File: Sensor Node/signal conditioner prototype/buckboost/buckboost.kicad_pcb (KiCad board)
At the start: 2 copper layers, 25.4 x 16 mm, 12 parts, among them J1 Conn_01x03_Pin, U9 TPS63000

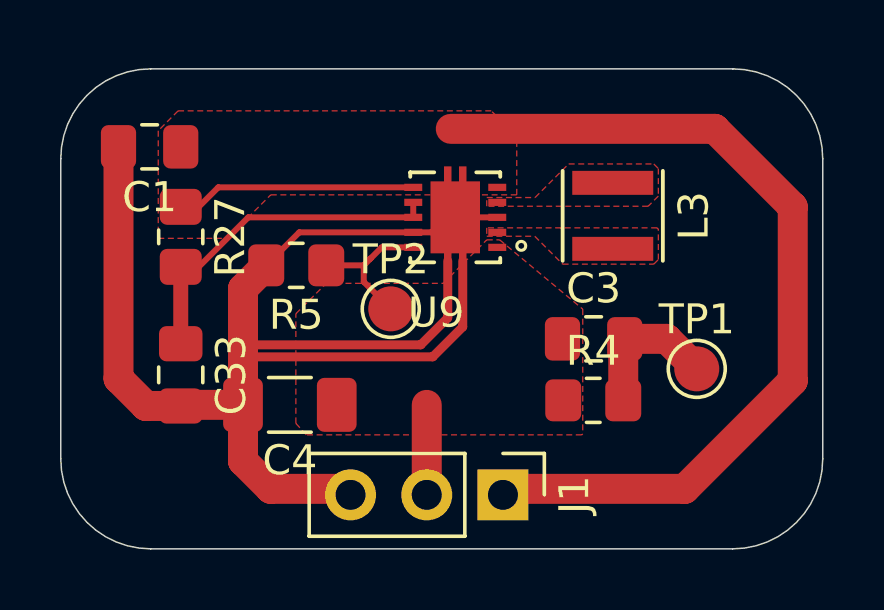
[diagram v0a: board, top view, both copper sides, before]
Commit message: Add finalized firmware - implemented power savings mode and implemented complete FSM.
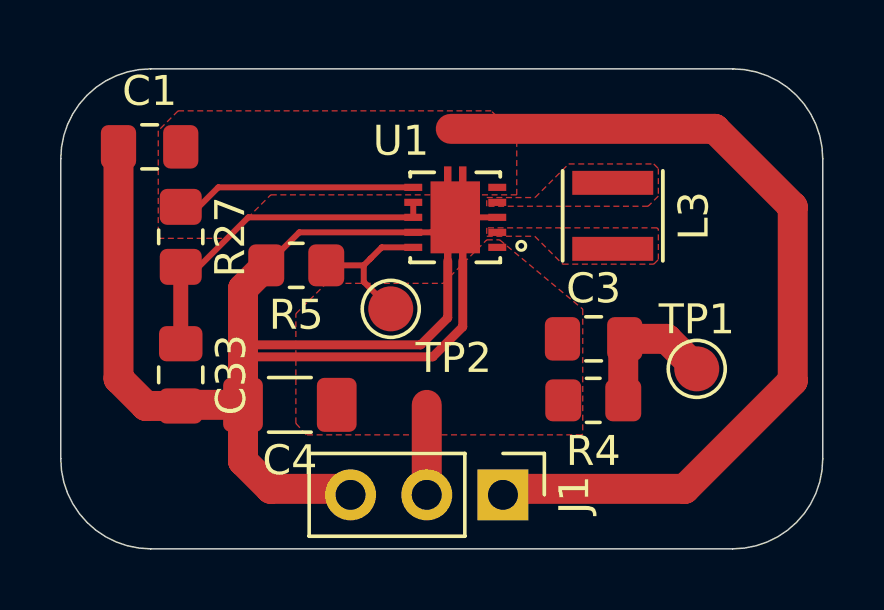
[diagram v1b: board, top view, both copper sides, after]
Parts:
- renumbered U9 to U1
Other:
- board text added: "C1"
- board text added: "C2"
- board text added: "C3"
- board text added: "C4"
- board text added: "L1"
- board text added: "R1"
- board text added: "R4"
- board text added: "R5"
- board text added: "TP1"
- board text added: "TP2"
- board text added: "U1"
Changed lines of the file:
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@@
 		(tags "test point SMD pad")
 		(property "Reference" "TP2"
-			(at 0 -1.648 0)
+			(at 2.1 1.64 0)
 			(layer "F.SilkS")
 			(effects
@@
 		(layer "F.Cu")
 		(at 118.75 71.15 180)
-		(property "Reference" "U9"
-			(at 0.635495 -3.177475 0)
+		(property "Reference" "U1"
+			(at 1.81 2.55 0)
 			(layer "F.SilkS")
 			(effects
@@
 		(tags "resistor handsolder")
 		(property "Reference" "R4"
-			(at 0 -1.65 0)
+			(at 0 1.69 0)
 			(layer "F.SilkS")
 			(effects
@@
 		(tags "capacitor handsolder")
 		(property "Reference" "C1"
-			(at 0 -1.68 0)
+			(at 0 1.86 0)
 			(layer "F.SilkS")
 			(effects
@@
 		(layer "Edge.Cuts")
 	)
+	(gr_text "L1"
+		(at 126.14 71.81 0)
+		(layer "User.3")
+		(effects
+			(font
+				(size 1 1)
+				(thickness 0.15)
+			)
+			(justify left bottom)
+		)
+	)
+	(gr_text "TP2"
+		(at 117.58 76.08 0)
+		(layer "User.3")
+		(effects
+			(font
+				(size 1 1)
+				(thickness 0.15)
+			)
+			(justify left bottom)
+		)
+	)
+	(gr_text "C2"
+		(at 106.35 76.97 0)
+		(layer "User.3")
+		(effects
+			(font
+				(size 1 1)
+				(thickness 0.15)
+			)
+			(justify left bottom)
+		)
+	)
+	(gr_text "R4"
+		(at 122.969199 79.65 0)
+		(layer "User.3")
+		(effects
+			(font
+				(size 1 1)
+				(thickness 0.15)
+			)
+			(justify left bottom)
+		)
+	)
+	(gr_text "R1"
+		(at 106.46 72.5 0)
+		(layer "User.3")
+		(effects
+			(font
+				(size 1 1)
+				(thickness 0.15)
+			)
+			(justify left bottom)
+		)
+	)
+	(gr_text "TP1"
+		(at 128.18 76.86 0)
+		(layer "User.3")
+		(effects
+			(font
+				(size 1 1)
+				(thickness 0.15)
+			)
+			(justify left bottom)
+		)
+	)
+	(gr_text "R5"
+		(at 112.48 75.18 0)
+		(layer "User.3")
+		(effects
+			(font
+				(size 1 1)
+				(thickness 0.15)
+			)
+			(justify left bottom)
+		)
+	)
+	(gr_text "C3"
+		(at 123 74.209627 0)
+		(layer "User.3")
+		(effects
+			(font
+				(size 1 1)
+				(thickness 0.15)
+			)
+			(justify left bottom)
+		)
+	)
+	(gr_text "C4"
+		(at 112.21 79.87 0)
+		(layer "User.3")
+		(effects
+			(font
+				(size 1 1)
+				(thickness 0.15)
+			)
+			(justify left bottom)
+		)
+	)
+	(gr_text "U1"
+		(at 116.02 69.01 0)
+		(layer "User.3")
+		(effects
+			(font
+				(size 1 1)
+				(thickness 0.15)
+			)
+			(justify left bottom)
+		)
+	)
+	(gr_text "C1"
+		(at 110.59 69.43 0)
+		(layer "User.3")
+		(effects
+			(font
+				(size 1 1)
+				(thickness 0.15)
+			)
+			(justify left bottom)
+		)
+	)
 	(segment
